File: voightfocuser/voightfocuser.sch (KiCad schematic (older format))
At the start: 9 parts

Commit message: added parts
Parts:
- removed U?: DRV8848, Package_SO:TSSOP-16-1EP_4.4x5mm_P0.65mm, symbol Driver_Motor:DRV8848
- added M?: Stepper_Motor_bipolar, symbol Motor:Stepper_Motor_bipolar
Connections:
- net labels added: GNDC, GNDD, VDD, ~RESET
- net labels removed: GND, GNDA
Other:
- note added: "Voight Focuser"
- moved on the sheet: SW?
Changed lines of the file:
@@
 U 1 1 5CDAD9A2
 P 800 2600
-F 0 "J?" H 857 3067 50  0000 C CNN
-F 1 "USB_B_Micro" H 857 2976 50  0000 C CNN
+F 0 "J?" H 650 3050 50  0000 C CNN
+F 1 "USB_B_Micro" H 850 2950 50  0000 C CNN
 F 2 "" H 950 2550 50  0001 C CNN
 F 3 "~" H 950 2550 50  0001 C CNN
@@
 	1    0    0    -1
 $EndComp
-Text GLabel 1900 1300 2    50   UnSpc ~ 0
-GNDA
-Text GLabel 1100 1150 2    50   UnSpc ~ 0
-GNDA
-Text GLabel 850  3000 2    50   UnSpc ~ 0
-GND
 Wire Wire Line
 	800  3000 850  3000
-Text GLabel 4900 6250 2    50   UnSpc ~ 0
-GND
 Wire Wire Line
 	4800 6200 4800 6250
@@
 Wire Wire Line
 	4900 3250 4950 3250
-Wire Wire Line
-	4700 3250 4100 3250
-Wire Wire Line
-	4100 3250 4100 3700
-Connection ~ 4700 3250
 $Comp
 L Regulator_Linear:AMS1117-5.0 U?
@@
 U 1 1 5CDD7FDC
 P 1850 4750
-F 0 "U?" H 1850 5631 50  0000 C CNN
-F 1 "FT230XS" H 1850 5540 50  0000 C CNN
+F 0 "U?" H 2100 5450 50  0000 C CNN
+F 1 "FT230XS" H 2200 5350 50  0000 C CNN
 F 2 "Package_SO:SSOP-16_3.9x4.9mm_P0.635mm" H 2300 4100 50  0001 C CNN
 F 3 "http://www.ftdichip.com/Products/ICs/FT230X.html" H 1850 4750 50  0001 C CNN
 	1    1850 4750
-	1    0    0    -1
-$EndComp
-$Comp
-L Driver_Motor:DRV8848 U?
-U 1 1 5CDD91C7
-P 5400 1650
-F 0 "U?" H 5400 2431 50  0000 C CNN
-F 1 "DRV8848" H 5400 2340 50  0000 C CNN
-F 2 "Package_SO:TSSOP-16-1EP_4.4x5mm_P0.65mm" H 5400 950 50  0001 C CNN
-F 3 "http://www.ti.com/lit/ds/symlink/drv8848.pdf" H 4250 3000 50  0001 C CNN
-	1    5400 1650
 	1    0    0    -1
 $EndComp
@@
 L Device:Rotary_Encoder_Switch SW?
 U 1 1 5CDDCFA9
-P 8800 1550
-F 0 "SW?" H 8800 1917 50  0000 C CNN
-F 1 "Rotary_Encoder_Switch" H 8800 1826 50  0000 C CNN
-F 2 "" H 8650 1710 50  0001 C CNN
-F 3 "~" H 8800 1810 50  0001 C CNN
-	1    8800 1550
+P 6700 5300
+F 0 "SW?" H 6700 5667 50  0000 C CNN
+F 1 "Rotary_Encoder_Switch" H 6700 5576 50  0000 C CNN
+F 2 "" H 6550 5460 50  0001 C CNN
+F 3 "~" H 6700 5560 50  0001 C CNN
+	1    6700 5300
 	1    0    0    -1
 $EndComp
@@
 	1    0    0    -1
 $EndComp
+$Comp
+L Motor:Stepper_Motor_bipolar M?
+U 1 1 5CDE265A
+P 6850 1500
+F 0 "M?" V 6818 1312 50  0000 R CNN
+F 1 "Stepper_Motor_bipolar" V 6727 1312 50  0000 R CNN
+F 2 "" H 6860 1490 50  0001 C CNN
+F 3 "http://www.infineon.com/dgdl/Application-Note-TLE8110EE_driving_UniPolarStepperMotor_V1.1.pdf?fileId=db3a30431be39b97011be5d0aa0a00b0" H 6860 1490 50  0001 C CNN
+	1    6850 1500
+	0    -1   -1   0
+$EndComp
+Text GLabel 1300 950  1    50   Input ~ 0
+VDD
+Text GLabel 5450 950  2    50   Input ~ 0
+VDD
+Text GLabel 1900 1300 2    50   Input ~ 0
+GNDC
+Text GLabel 1100 1150 2    50   Input ~ 0
+GNDD
+Text GLabel 850  3000 2    50   Input ~ 0
+GNDC
+Text GLabel 700  3000 3    50   Input ~ 0
+GNDC
+Text GLabel 1100 2400 2    50   Input ~ 0
+VCC
+Text GLabel 5450 2350 3    50   Input ~ 0
+GNDD
+Text GLabel 5550 2350 3    50   Input ~ 0
+GNDD
+Text GLabel 4900 6250 2    50   Input ~ 0
+GNDC
+Text GLabel 1850 7050 2    50   Input ~ 0
+GNDC
+Wire Wire Line
+	1750 5450 1950 5450
+Wire Wire Line
+	1950 5450 2050 5450
+Connection ~ 1950 5450
+Text GLabel 2050 5450 2    50   Input ~ 0
+GNDC
+Text GLabel 1750 4050 1    50   Input ~ 0
+VCC
+Text GLabel 1950 4050 1    50   Input ~ 0
+VCC
+Text GLabel 4100 3700 0    50   Input ~ 0
+~RESET
+Text GLabel 1150 4950 0    50   Input ~ 0
+~RESET
+Text Notes 7000 7050 0    354  ~ 0
+Voight Focuser
 $EndSCHEMATC

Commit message: datasheets
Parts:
- added U?: DRV8825, Package_SO:HTSSOP-28-1EP_4.4x9.7mm_P0.65mm_EP3.4x9.5mm_Mask2.4x6.17mm_ThermalVias, symbol JeffLibrary:DRV8825
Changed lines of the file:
@@
 Text GLabel 1300 950  1    50   Input ~ 0
-VDD
-Text GLabel 5450 950  2    50   Input ~ 0
 VDD
 Text GLabel 1900 1300 2    50   Input ~ 0
@@
 Text GLabel 1100 2400 2    50   Input ~ 0
 VCC
-Text GLabel 5450 2350 3    50   Input ~ 0
-GNDD
-Text GLabel 5550 2350 3    50   Input ~ 0
-GNDD
 Text GLabel 4900 6250 2    50   Input ~ 0
 GNDC
@@
 Text Notes 7000 7050 0    354  ~ 0
 Voight Focuser
+$Comp
+L JeffLibrary:DRV8825 U?
+U 1 1 5CDE1BDD
+P 4650 1550
+F 0 "U?" H 4675 2425 50  0000 C CNN
+F 1 "DRV8825" H 4675 2334 50  0000 C CNN
+F 2 "Package_SO:HTSSOP-28-1EP_4.4x9.7mm_P0.65mm_EP3.4x9.5mm_Mask2.4x6.17mm_ThermalVias" H 4750 650 50  0001 C CNN
+F 3 "http://www.ti.com/lit/ds/symlink/drv8825.pdf" H 4500 2200 50  0001 C CNN
+	1    4650 1550
+	1    0    0    -1
+$EndComp
+Wire Notes Line
+	8800 2050 8800 4050
+Wire Notes Line
+	8800 4050 10450 4050
+Wire Notes Line
+	10450 4050 10450 2050
+Wire Notes Line
+	10450 2050 8800 2050
 $EndSCHEMATC

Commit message: datasheets
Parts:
- added C?: CP, symbol Device:CP
- U?: value AMS1117-5.0 -> AMS1117-3.3
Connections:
- net GNDC: now also C?.2
- net GNDD: now also U?.25 (MODE1)
- net VCC: no longer U?.12 (VCC), U?.2 (VO), U?.3 (VCCIO), U?.31 (UVCC), U?.32 (AVCC), U?.4 (VCC)
- net D-: now reaches J?.2 (D-)
- net D-: now also U?.9 (USBDM)
- net D+: now reaches J?.3 (D+)
- net D+: now also U?.8 (USBDP)
- net TXD: now reaches U?.1 (TXD)
- net ~RTS: now reaches U?.2 (~RTS)
- net RXD: now reaches U?.4 (RXD)
- net ~CTS: now reaches U?.6 (~CTS)
- net VCC3.3: now reaches U?.8 (+Vs)
- net VCC3.3: now also U?.31 (UVCC), U?.32 (AVCC), U?.4 (VCC)
- new net VCC3,3: U?.12 (VCC)
- new net VCC5+: C?.1, U?.2 (VO)
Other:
- note added: "Should be isolated from heat. Back of board on own ground plane."
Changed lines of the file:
@@
 Connection ~ 4800 6250
 Text GLabel 2500 950  2    50   UnSpc ~ 0
-VCC
+VCC5+
 Text GLabel 4950 3250 2    50   UnSpc ~ 0
-VCC
+VCC3.3
 Wire Wire Line
 	4700 3400 4700 3250
@@
 P 1850 950
 F 0 "U?" H 1850 1192 50  0000 C CNN
-F 1 "AMS1117-5.0" H 1850 1101 50  0000 C CNN
+F 1 "AMS1117-3.3" H 1850 1101 50  0000 C CNN
 F 2 "Package_TO_SOT_SMD:SOT-223-3_TabPin2" H 1850 1150 50  0001 C CNN
 F 3 "http://www.advanced-monolithic.com/pdf/ds1117.pdf" H 1950 700 50  0001 C CNN
@@
 	1850 1300 1900 1300
 Wire Wire Line
-	2150 950  2500 950
+	2150 950  2400 950
 $Comp
 L Interface_USB:FT230XS U?
@@
 GNDC
 Text GLabel 1750 4050 1    50   Input ~ 0
-VCC
-Text GLabel 1950 4050 1    50   Input ~ 0
-VCC
+VCC3,3
 Text GLabel 4100 3700 0    50   Input ~ 0
 ~RESET
@@
 Wire Notes Line
 	10450 2050 8800 2050
+$Comp
+L Device:CP C?
+U 1 1 5CE22235
+P 2400 1200
+F 0 "C?" H 2518 1246 50  0000 L CNN
+F 1 "CP" H 2518 1155 50  0000 L CNN
+F 2 "" H 2438 1050 50  0001 C CNN
+F 3 "~" H 2400 1200 50  0001 C CNN
+	1    2400 1200
+	1    0    0    -1
+$EndComp
+Wire Wire Line
+	2400 1050 2400 950
+Connection ~ 2400 950
+Wire Wire Line
+	2400 950  2500 950
+Text GLabel 2500 1500 2    50   Input ~ 0
+GNDC
+Wire Wire Line
+	2400 1350 2400 1500
+Wire Wire Line
+	2400 1500 2500 1500
+Wire Wire Line
+	1050 1150 1050 1300
+Wire Wire Line
+	1050 1300 1850 1300
+Connection ~ 1850 1300
+Text GLabel 1300 2600 2    50   Input ~ 0
+D+
+Text GLabel 1300 2700 2    50   Input ~ 0
+D-
+Wire Wire Line
+	1100 2600 1300 2600
+Wire Wire Line
+	1100 2700 1300 2700
+Text GLabel 5300 900  2    50   Input ~ 0
+GNDD
+Wire Wire Line
+	5100 900  5300 900
+Text GLabel 2150 6000 2    50   Input ~ 0
+VCC3.3
+Wire Wire Line
+	1850 6050 1850 6000
+Wire Wire Line
+	1850 6000 2150 6000
+Text GLabel 1050 4750 0    50   Input ~ 0
+D+
+Text GLabel 1050 4650 0    50   Input ~ 0
+D-
+Wire Wire Line
+	1150 4650 1050 4650
+Wire Wire Line
+	1150 4750 1050 4750
+Text GLabel 2850 4350 2    50   Input ~ 0
+TXD
+Text GLabel 2650 4450 2    50   Input ~ 0
+RXD
+Text GLabel 2850 4550 2    50   Input ~ 0
+~RTS
+Text GLabel 2650 4650 2    50   Input ~ 0
+~CTS
+Wire Wire Line
+	2550 4350 2850 4350
+Wire Wire Line
+	2550 4450 2650 4450
+Wire Wire Line
+	2550 4550 2850 4550
+Wire Wire Line
+	2550 4650 2650 4650
+Wire Notes Line
+	1100 5750 2600 5750
+Wire Notes Line
+	2600 5750 2600 7150
+Wire Notes Line
+	2600 7150 1100 7150
+Wire Notes Line
+	1100 5750 1100 7150
+Text Notes 3150 5750 2    50   ~ 0
+Should be isolated from heat. Back of board on own ground plane.
 $EndSCHEMATC

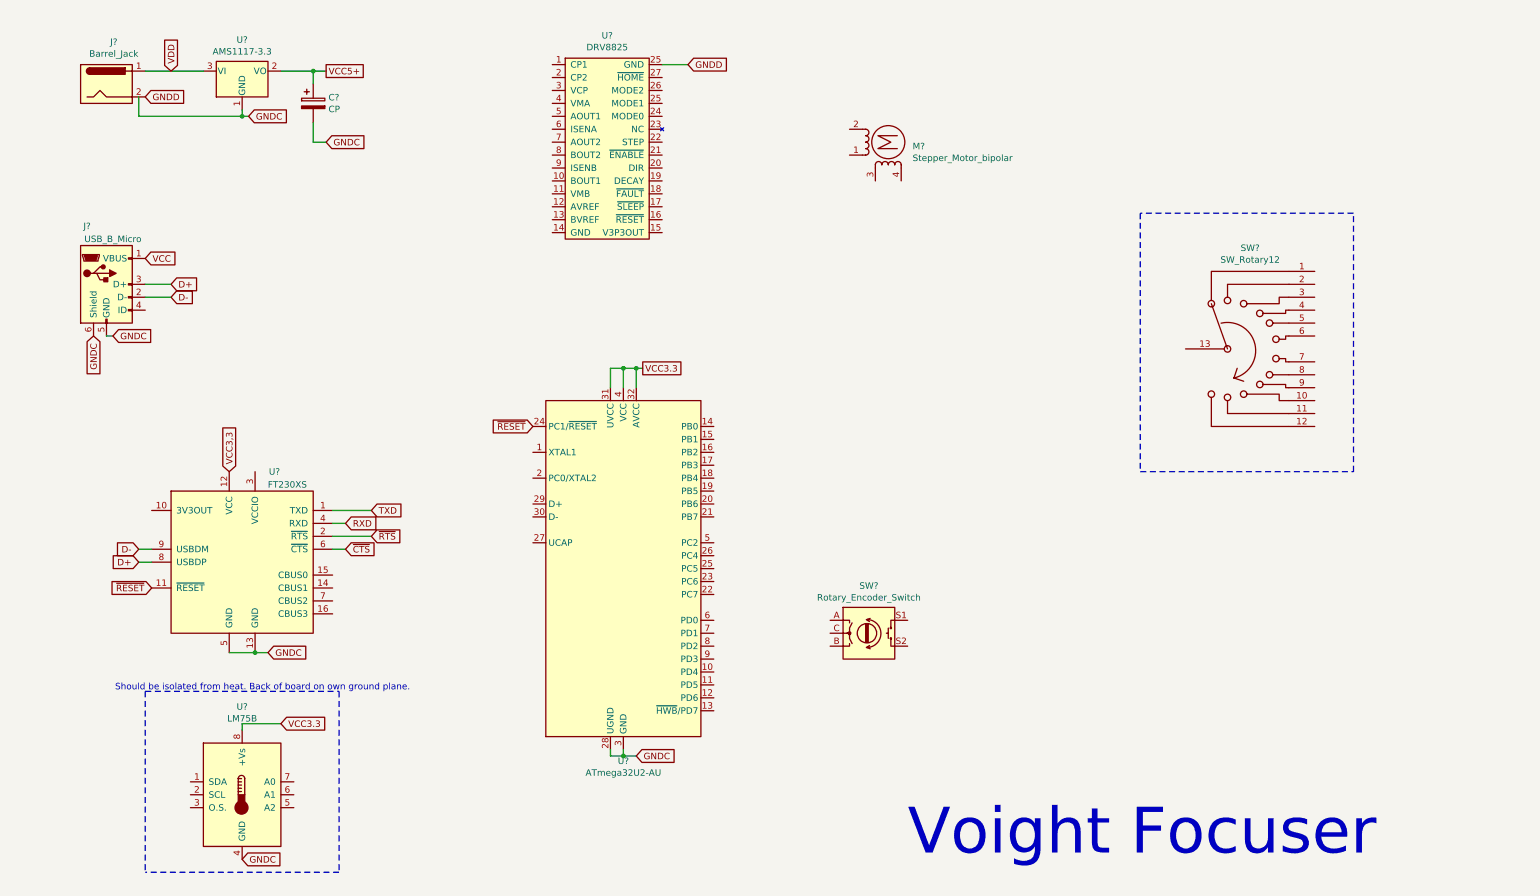
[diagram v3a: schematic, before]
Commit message: adding resistors and caps to drv8825
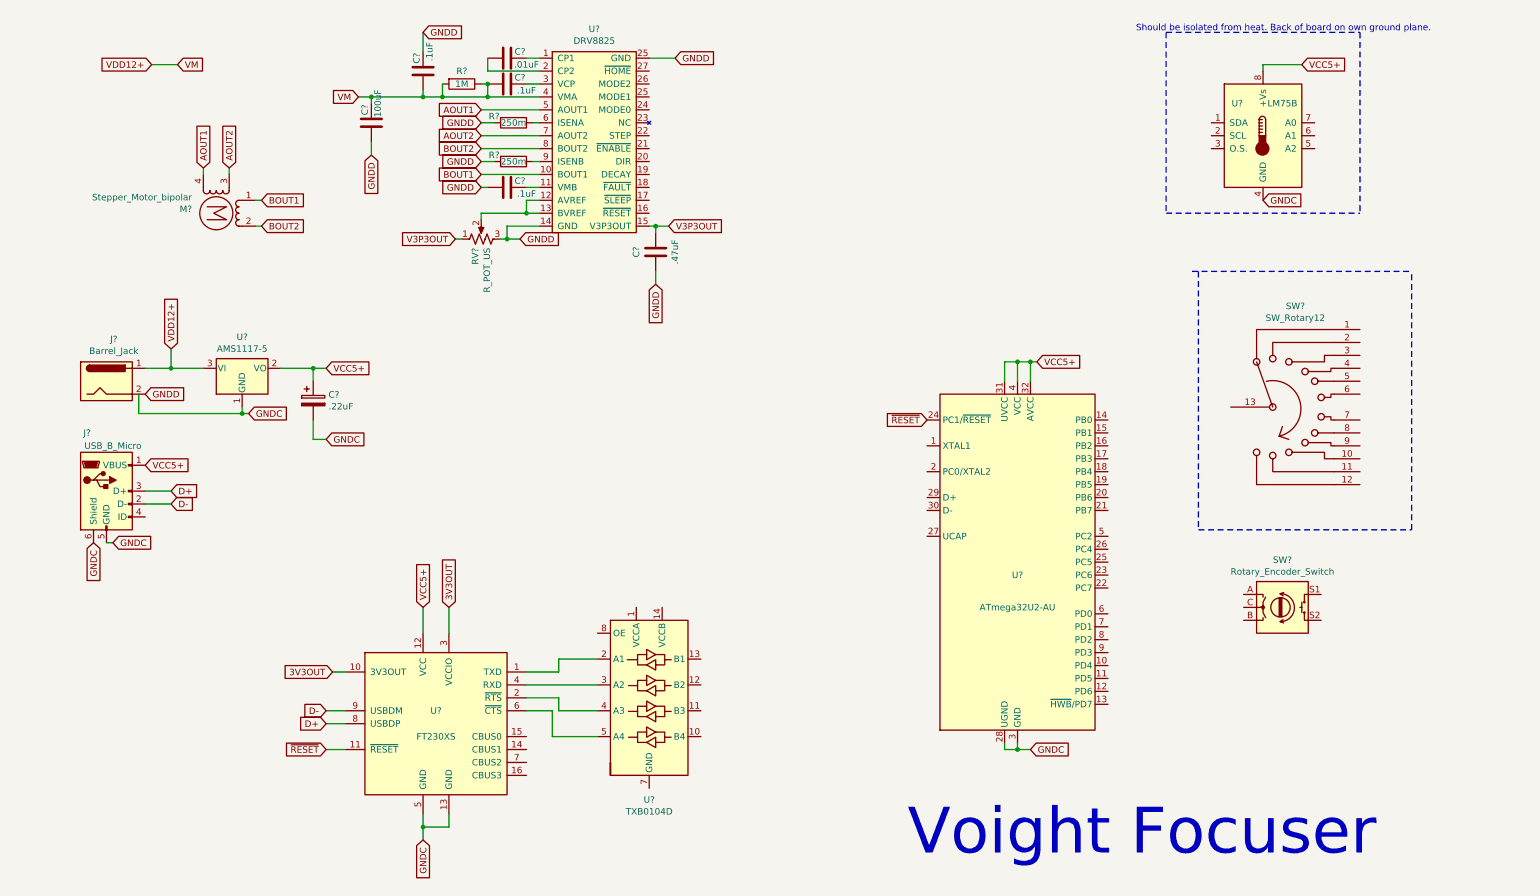
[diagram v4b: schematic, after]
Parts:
- removed U?: FT230XS, Package_SO:SSOP-16_3.9x4.9mm_P0.635mm, symbol Interface_USB:FT230XS
- added C?: .01uF, symbol Device:C
- added C? (x3): .1uF, symbol Device:C
- added C?: 100uF, symbol Device:C
- added C?: .47uF, symbol Device:C
- added R?: 1M, symbol Device:R
- added R? (x2): 250m, symbol Device:R
- added RV?: R_POT_US, symbol Device:R_POT_US
- added U?: TXB0104D, Package_SO:SOIC-14_3.9x8.7mm_P1.27mm, symbol Logic_LevelTranslator:TXB0104D
- added U?: FT230XS, Package_SO:SSOP-16_3.9x4.9mm_P0.635mm, symbol Interface_USB:FT230XS
- C?: value CP -> .22uF
- U?: value AMS1117-3.3 -> AMS1117-5
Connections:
- net VCC is gone; now on net VCC5+: J?.1 (VBUS)
- net VCC3.3 is gone; now on net VCC5+: U?.31 (UVCC), U?.32 (AVCC), U?.4 (VCC), U?.8 (+Vs)
- net VDD is gone; now on net VDD12+: J?.1, U?.3 (VI)
- net D+: now also U?.8 (USBDP)
- net D-: now also U?.9 (USBDM)
- net GNDC: now also U?.13 (GND), U?.5 (GND)
- net GNDD: now also U?.14 (GND), C?.1, C?.2, C?.2, C?.2, R?.2, R?.2, RV?.3
- net VCC5+: now also U?.12 (VCC)
- net ~RESET: now also U?.11 (~RESET)
- net at U?.1 (CP1): now also C?.1
- net BOUT1: now reaches U?.10 (BOUT1)
- net BOUT1: now also M?.1
- net at U?.11 (VMB): now also C?.1
- net at U?.12 (AVREF): now also U?.13 (BVREF), RV?.2
- net V3P3OUT: now reaches U?.15 (V3P3OUT)
- net V3P3OUT: now also C?.1, RV?.1
- net at U?.2 (CP2): now also C?.2
- net at U?.3 (VCP): now also C?.1
- net VDD12+: now reaches U?.4 (VMA)
- net VDD12+: now also C?.1, C?.2, C?.2, R?.1, R?.2
- net AOUT1: now reaches U?.5 (AOUT1)
- net AOUT1: now also M?.4
- net at U?.6 (ISENA): now also R?.1
- net AOUT2: now reaches U?.7 (AOUT2)
- net AOUT2: now also M?.3
- net BOUT2: now reaches U?.8 (BOUT2)
- net BOUT2: now also M?.2 (-)
- net at U?.9 (ISENB): now also R?.1
- new net: U?.1 (TXD), U?.2 (A1)
- new net: U?.3 (A2), U?.4 (RXD)
- new net: U?.2 (~RTS), U?.4 (A3)
- new net: U?.5 (A4), U?.6 (~CTS)
- new net 3V3OUT: U?.10 (3V3OUT), U?.3 (VCCIO)
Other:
- moved on the sheet: C?, J?, M?, SW?, U?

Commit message: more components. switch 328p in
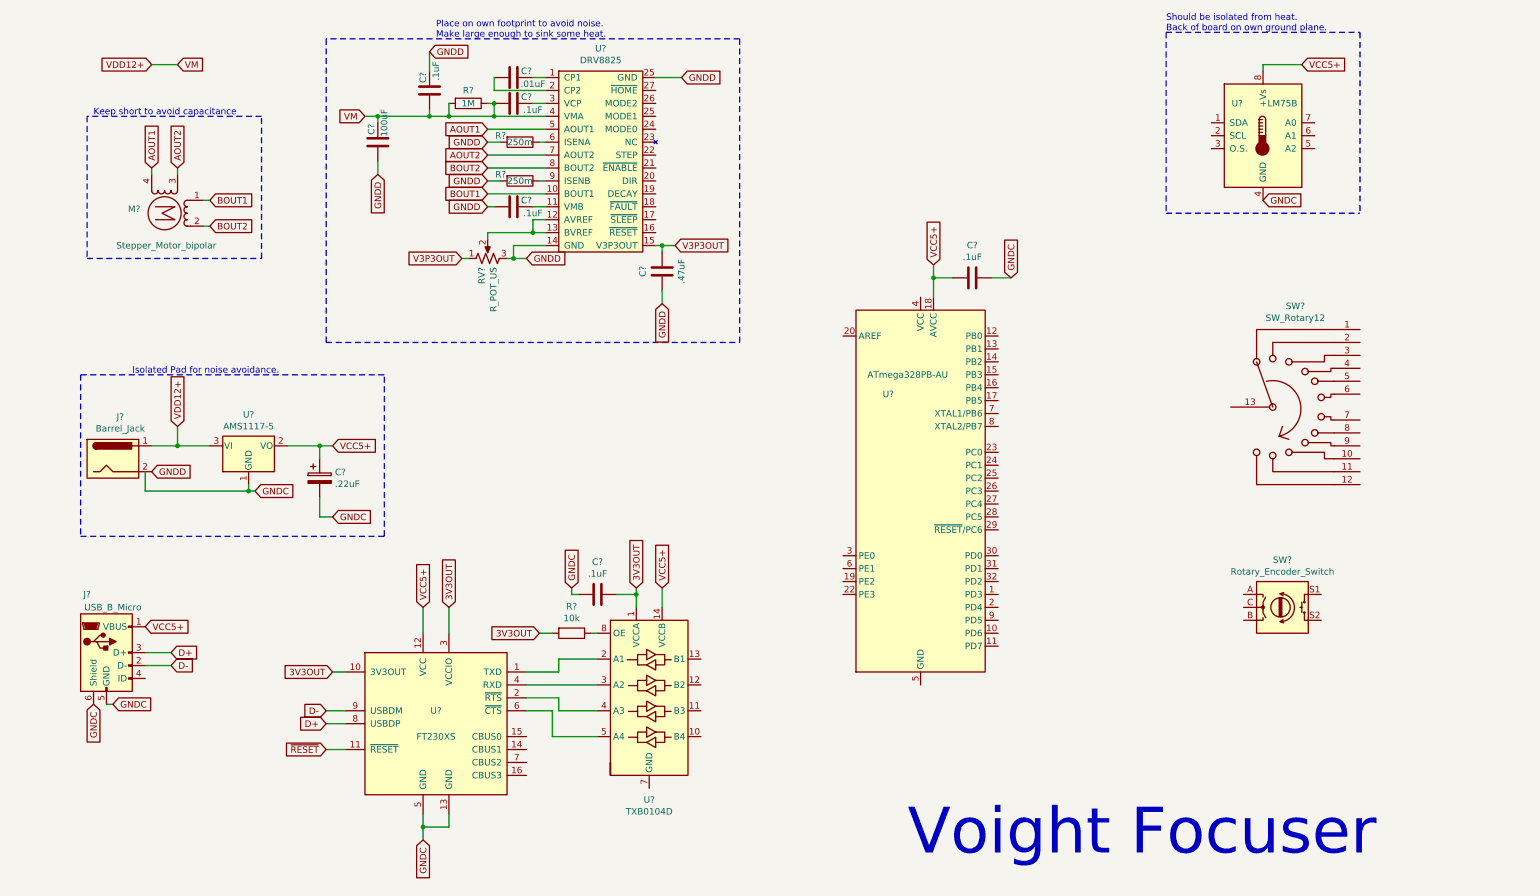
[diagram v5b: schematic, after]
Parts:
- removed U?: ATmega32U2-AU, Package_QFP:TQFP-32_7x7mm_P0.8mm, symbol MCU_Microchip_ATmega:ATmega32U2-AU
- added C? (x2): .1uF, symbol Device:C
- added R?: 10k, symbol Device:R
- added U?: ATmega328PB-AU, Package_QFP:TQFP-32_7x7mm_P0.8mm, symbol MCU_Microchip_ATmega:ATmega328PB-AU
- M?: footprint (none) -> Connector_PinHeader_2.54mm:PinHeader_1x04_P2.54mm_Vertical
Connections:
- net 3V3OUT: now also U?.1 (VCCA), C?.1, R?.2
- net GNDC: now also C?.1, C?.2
- net VCC5+: now also U?.14 (VCCB), C?.2, U?.18 (AVCC)
- net at U?.8 (OE): now also R?.1
- new net: U?.21 (GND), U?.5 (GND)
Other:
- note added: "Isolated Pad for noise avoidance."
- note added: "Keep short to avoid capacitance"
- note added: "Place on own footprint to avoid noise.\nMake large enough to sink some heat."
- note added: "Should be isolated from heat.\nBack of board on own ground plane."
- note removed: "Should be isolated from heat. Back of board on own ground plane."
- moved on the sheet: C?, J?, M?, R?, RV?, U?
